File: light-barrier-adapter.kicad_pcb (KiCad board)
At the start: 2 copper layers, 41.3 x 14.9 mm, 4 parts, among them J1 Conn_PinHeader_1x05_P2.54mm_V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, J2 Conn_PinHeader_1x03_P2.54mm_V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

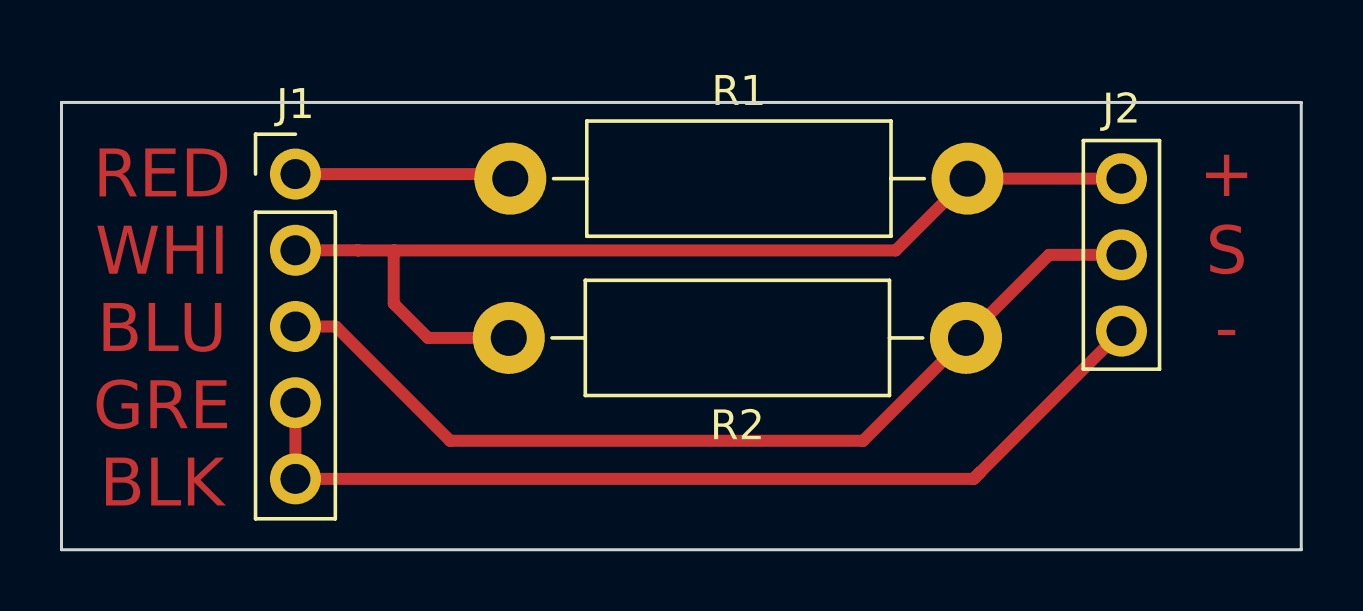
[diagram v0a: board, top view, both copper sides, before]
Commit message: feat(): make board smaller
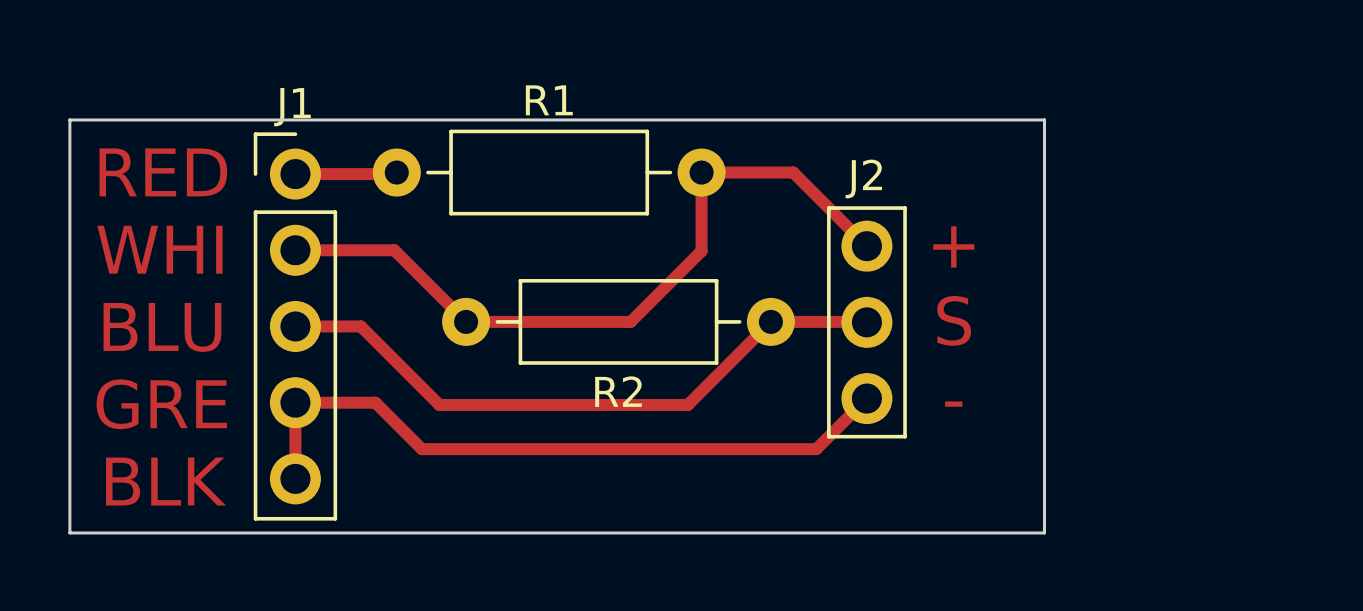
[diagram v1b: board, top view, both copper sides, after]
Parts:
- R1, R2: footprint Resistor_THT:R_Axial_DIN0411_L9.9mm_D3.6mm_P15.24mm_Horizontal -> Resistor_THT:R_Axial_DIN0207_L6.3mm_D2.5mm_P10.16mm_Horizontal
- moved J2 8.78 mm to (148.3, 86.4)
- moved R2 6.52 mm to (145.1, 88.9)
- moved R1 3.79 mm to (132.7, 83.9)
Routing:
- net /LB_S: track 31.7 -> 21.3 mm
- net /LB_VCC: track 34.7 -> 24.7 mm
- net /LB_GND: track 32.4 -> 22.9 mm
- net /LB_ANODE: track 7.23 -> 3.40 mm
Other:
- board size 41.3 x 14.9 mm -> 32.5 x 13.8 mm
